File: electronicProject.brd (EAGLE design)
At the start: 100.3 x 79.7 mm, 15 parts

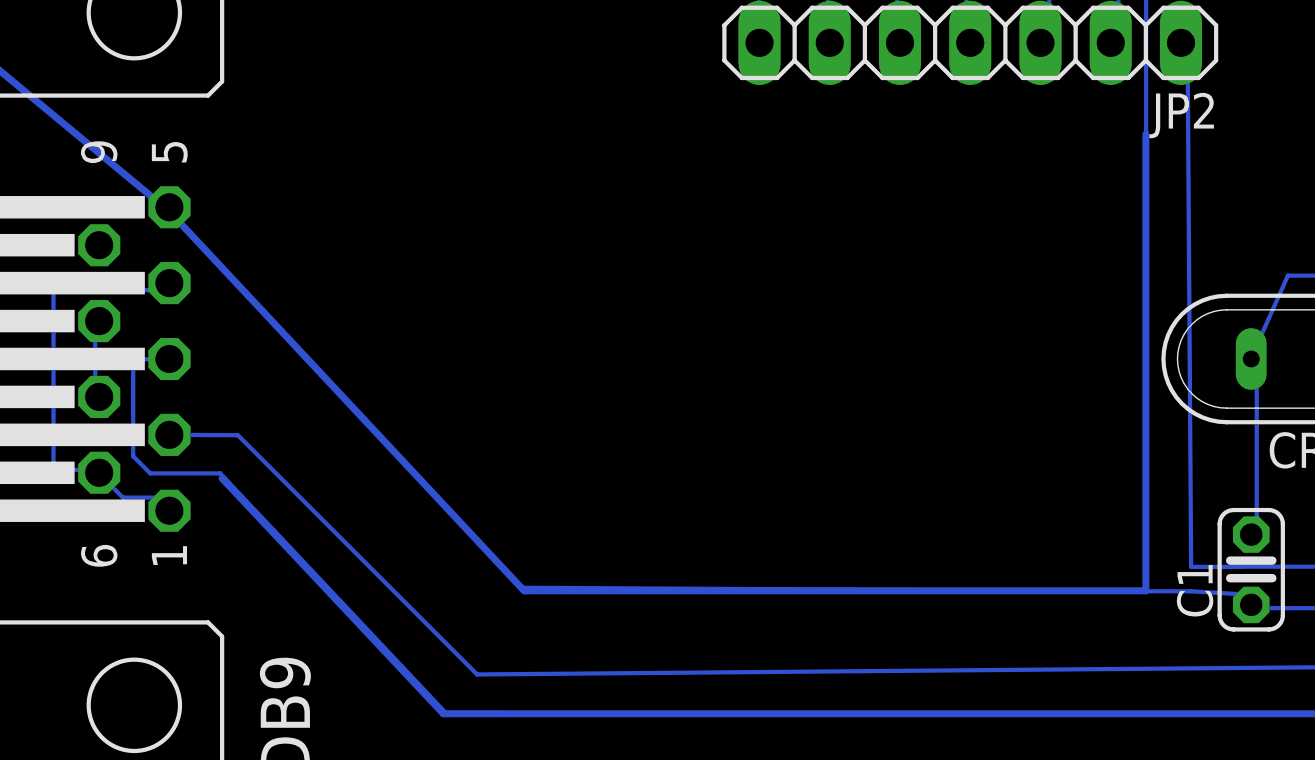
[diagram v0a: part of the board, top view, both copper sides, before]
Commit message: Update PCB design
Add Group and names on PCB
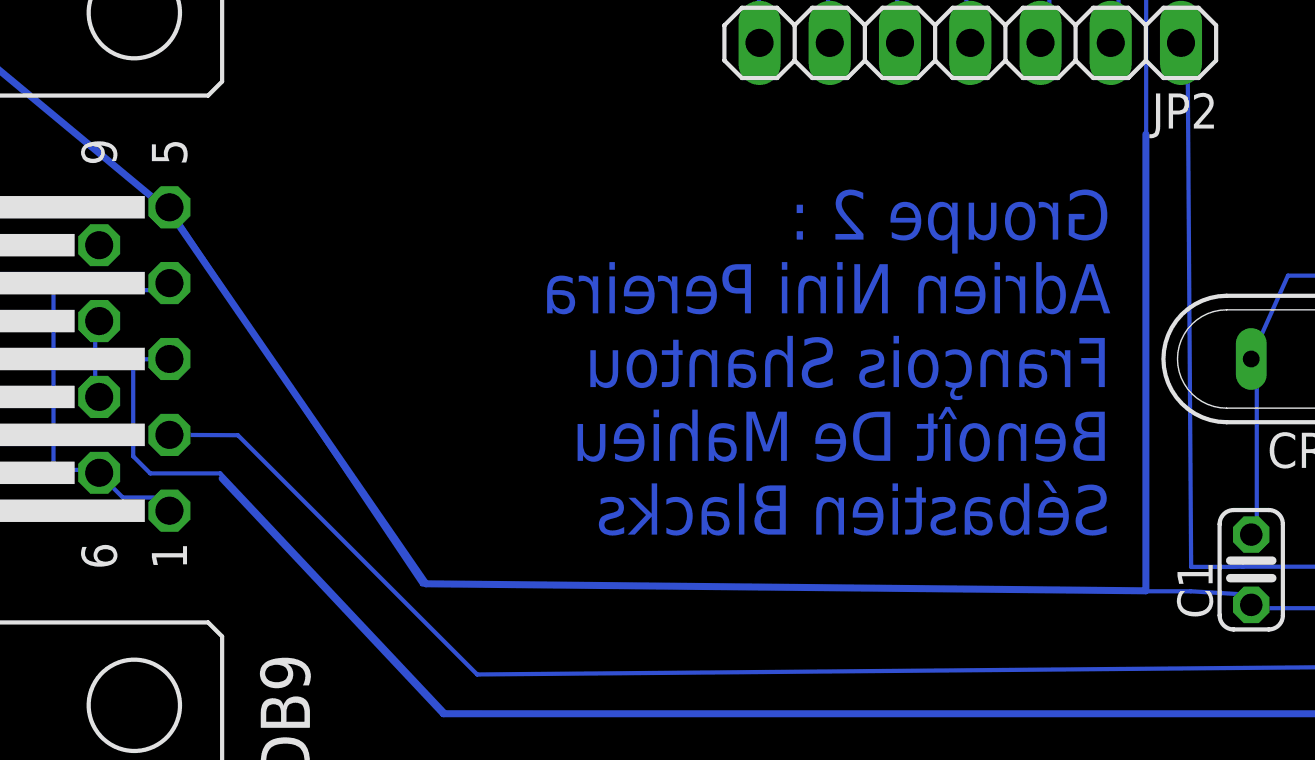
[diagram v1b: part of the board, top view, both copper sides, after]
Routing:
- net GND: track 630.3 -> 632.7 mm
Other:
- board text added: "Groupe 2 : Adrien Nini Pereira François Shantou Benoît De Mahieu Sébastien Blacks"
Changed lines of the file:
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@@
 </layers>
 <board>
+<fusionsync huburn="a.cGVyc29uYWw6dWUyYTAzMjA4" projecturn="a.cGVyc29uYWw6dWUyYTAzMjA4IzIwMTgwMjI2MTE5OTU2ODMx" f3durn="urn:adsk.wipprod:dm.lineage:Xcq5O81EQeOARa1FyexisA" pcbguid="bc2aa3ce-9b05-49e0-8871-5361d34968a8" lastpulledtime="" lastsyncedchangeguid="d90ede07-6539-4036-15fc-433ef894a95e"/>
 <plain>
 <wire x1="0" y1="0" x2="100.31" y2="0" width="0" layer="20"/>
@@
 <wire x1="100.31" y1="79.68" x2="0" y2="79.68" width="0" layer="20"/>
 <wire x1="0" y1="79.68" x2="0" y2="0" width="0" layer="20"/>
+<text x="45.72" y="10.16" size="1.778" layer="16" rot="MR0">Groupe 2 :
+Adrien Nini Pereira
+François Shantou
+Benoît De Mahieu
+Sébastien Blacks</text>
 </plain>
 <attributes>
@@
 <wire x1="14.5" y1="44" x2="14.6812" y2="44.1706" width="0.1524" layer="16"/>
 <wire x1="48.611" y1="8.111" x2="50.5" y2="8" width="0.1524" layer="16"/>
-<wire x1="24.373" y1="8.238" x2="47" y2="8.111" width="0.1524" layer="16"/>
+<wire x1="20.817" y1="8.365" x2="47" y2="8.111" width="0.1524" layer="16"/>
 <wire x1="47" y1="8.111" x2="48.611" y2="8.111" width="0.1524" layer="16"/>
-<wire x1="12" y1="21.5" x2="24.373" y2="8.238" width="0.1524" layer="16"/>
+<wire x1="12" y1="21.5" x2="20.817" y2="8.365" width="0.1524" layer="16"/>
 <wire x1="50.5" y1="8" x2="50.8" y2="7.62" width="0.1524" layer="16"/>
 <wire x1="12" y1="21.5" x2="11.684" y2="21.9964" width="0.1524" layer="16"/>
@@
 <wire x1="5.08" y1="41.656" x2="4.953" y2="27.432" width="0.254" layer="16"/>
 <wire x1="4.953" y1="27.432" x2="11.684" y2="21.844" width="0.254" layer="16"/>
-<wire x1="11.684" y1="21.844" x2="24.511" y2="8.128" width="0.254" layer="16"/>
-<wire x1="24.511" y1="8.128" x2="46.99" y2="8.128" width="0.254" layer="16"/>
+<wire x1="11.684" y1="21.844" x2="20.955" y2="8.382" width="0.254" layer="16"/>
+<wire x1="20.955" y1="8.382" x2="46.99" y2="8.128" width="0.254" layer="16"/>
 <wire x1="46.99" y1="8.128" x2="46.99" y2="24.638" width="0.254" layer="16"/>
 <wire x1="95.25" y1="36.83" x2="91.44" y2="36.83" width="0.254" layer="16"/>
@@
 </drawing>
 <compatibility>
+<note version="6.3" minversion="6.2.2" severity="warning">
+Since Version 6.2.2 text objects can contain more than one line,
+which will not be processed correctly with this version.
+</note>
 <note version="8.2" severity="warning">
 Since Version 8.2, EAGLE supports online libraries. The ids
@@
 </note>
 <note version="8.3" severity="warning">
+Since Version 8.3, EAGLE supports Fusion synchronisation.
+This feature will not be available in this version and saving
+the document will break the link to the Fusion PCB feature.
+</note>
+<note version="8.3" severity="warning">

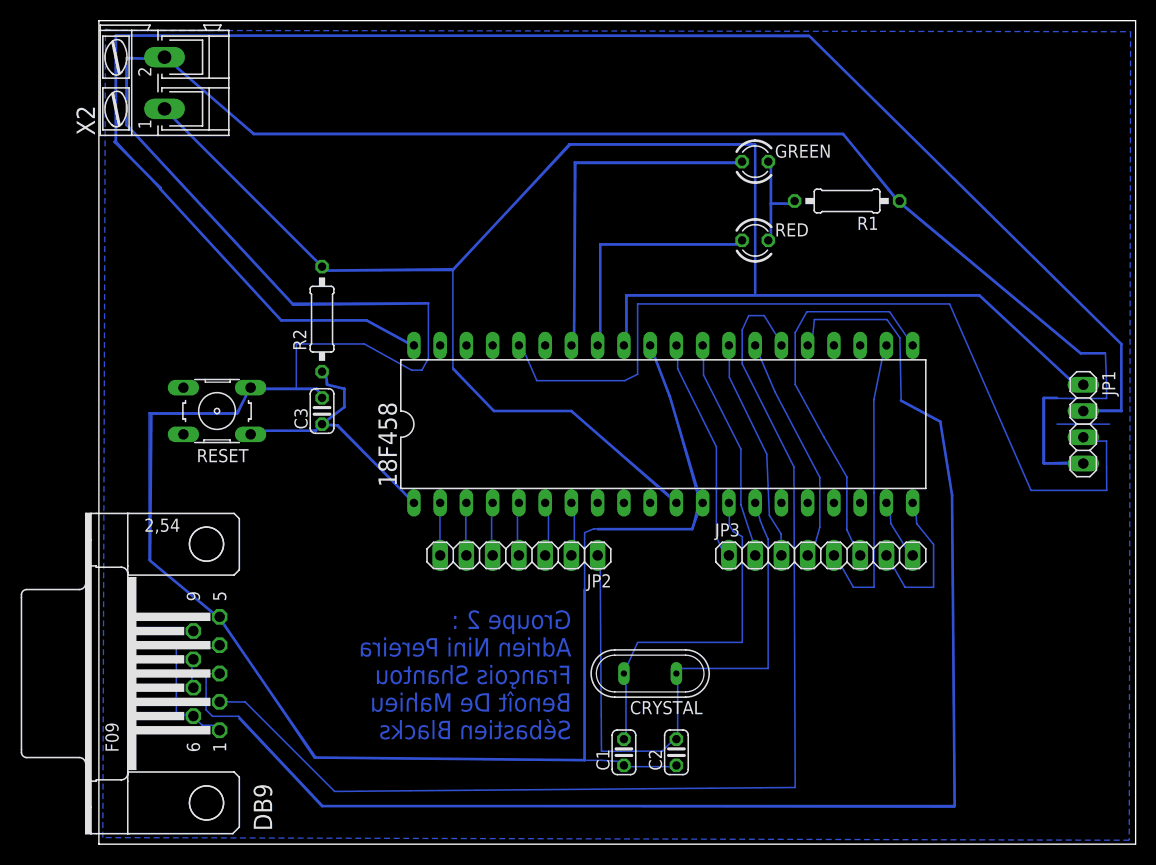
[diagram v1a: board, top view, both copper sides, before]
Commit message: Board UPDATE
Correction sonde à ultrasons (rotation 180°)
Reroutage des pattes de la sonde
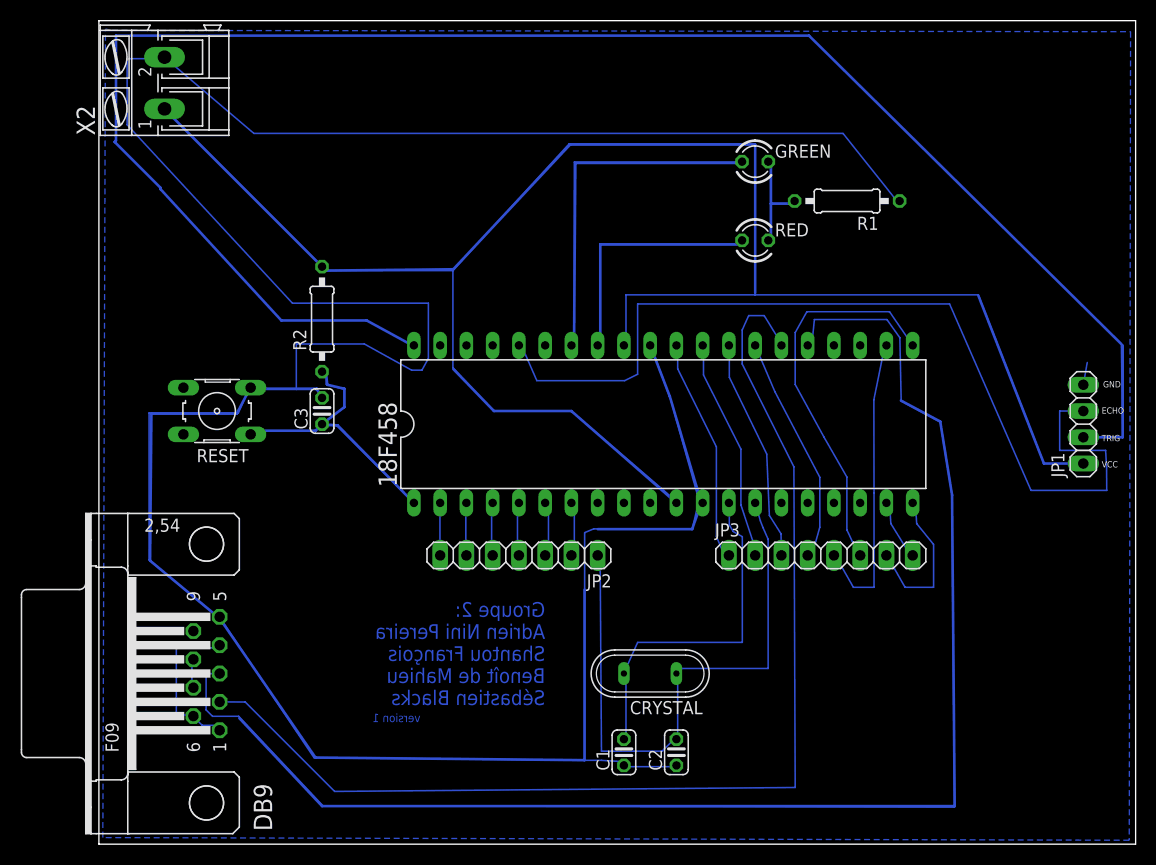
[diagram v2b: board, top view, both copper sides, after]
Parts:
- turned JP1 to 90 degrees
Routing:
- net GND: track 632.7 -> 423.1 mm
- net N$13: track 114.1 -> 0.00 mm
- net TRIG: track 219.3 -> 178.3 mm
- net VCC: track 320.4 -> 293.1 mm
- net ECHO: track 85.0 -> 92.2 mm
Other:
- board text added: "ECHO"
- board text added: "GND"
- board text added: "Groupe 2: Adrien Nini Pereira Shantou François Benoît de Mahieu Sébastien Blacks"
- board text added: "TRIG"
- board text added: "VCC"
- board text added: "version 1"
- board text removed: "Groupe 2 : Adrien Nini Pereira François Shantou Benoît De Mahieu Sébastien Blacks"

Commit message: final design
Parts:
- JP2: device pinhead:1X07 -> pinhead:1X06
- moved JP2 1.27 mm to (39.4, 27.9)
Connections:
- net N$10: now also JP2.3; no longer JP2.4
- net N$14: now also JP2.2; no longer JP2.3
- net N$15: now also JP2.1; no longer JP2.2
- net N$17: no longer JP2.1
- net N$4: now also JP2.6; no longer JP2.7
- net N$5: now also JP2.5; no longer JP2.6
- net N$6: now also JP2.4; no longer JP2.5
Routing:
- net N$17: track 58.7 -> 39.7 mm
- net N$10: track 5.29 -> 10.5 mm
- net N$6: track 5.22 -> 10.3 mm
- net N$5: track 5.15 -> 10.2 mm
- net N$4: track 5.09 -> 10.2 mm
- net N$14: track 5.65 -> 10.6 mm
- net N$15: track 5.57 -> 10.5 mm
- net TRIG: track 178.3 -> 178.9 mm
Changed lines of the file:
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@@
 </element>
 <element name="JP3" library="pinhead" library_urn="urn:adsk.eagle:library:325" package="1X08" package3d_urn="urn:adsk.eagle:package:22409/2" value="" x="69.85" y="27.94"/>
-<element name="JP2" library="pinhead" library_urn="urn:adsk.eagle:library:325" package="1X07" package3d_urn="urn:adsk.eagle:package:22477/2" value="" x="40.64" y="27.94" rot="R180"/>
+<element name="JP2" library="pinhead" library_urn="urn:adsk.eagle:library:325" package="1X06" package3d_urn="urn:adsk.eagle:package:22472/2" value="" x="39.37" y="27.94" rot="R180"/>
 </elements>
 <signals>
@@
 <wire x1="5.969" y1="63.373" x2="17.653" y2="50.673" width="0.254" layer="16"/>
 <wire x1="17.653" y1="50.673" x2="25.908" y2="50.673" width="0.254" layer="16"/>
-<wire x1="25.908" y1="50.673" x2="30.099" y2="48.387" width="0.254" layer="16"/>
-<wire x1="30.48" y1="48.26" x2="30.099" y2="48.387" width="0" layer="19" extent="16-16"/>
+<wire x1="25.908" y1="50.673" x2="29.975196875" y2="48.454528125" width="0.254" layer="16"/>
+<wire x1="29.975196875" y1="48.454528125" x2="30.099" y2="48.387" width="0.254" layer="16"/>
+<wire x1="30" y1="48.5" x2="30.25" y2="48.5" width="0.1524" layer="16"/>
+<wire x1="30.25" y1="48.5" x2="30.48" y2="48.26" width="0.1524" layer="16"/>
+<wire x1="30" y1="48.5" x2="29.975196875" y2="48.454528125" width="0.1524" layer="16"/>
 </signal>
 <signal name="ECHO">
@@
 <wire x1="82.532" y1="33.881" x2="81.413" y2="40.842" width="0.1524" layer="16"/>
 <wire x1="82.786" y1="3.587" x2="82.532" y2="33.881" width="0.1524" layer="16"/>
-<wire x1="21.675" y1="3.714" x2="82.786" y2="3.587" width="0.1524" layer="16"/>
+<wire x1="21.675" y1="3.714" x2="40.999840625" y2="3.673840625" width="0.1524" layer="16"/>
+<wire x1="40.999840625" y1="3.673840625" x2="82.786" y2="3.587" width="0.1524" layer="16"/>
 <wire x1="13.524" y1="12.373" x2="21.675" y2="3.714" width="0.1524" layer="16"/>
 <wire x1="10.992" y1="12.373" x2="13.524" y2="12.373" width="0.1524" layer="16"/>
@@
 <wire x1="11.5" y1="16.5" x2="11.684" y2="16.51" width="0.1524" layer="16"/>
 <wire x1="13.589" y1="12.192" x2="21.59" y2="3.683" width="0.254" layer="16"/>
-<wire x1="21.59" y1="3.683" x2="82.804" y2="3.683" width="0.254" layer="16"/>
+<wire x1="21.59" y1="3.683" x2="41" y2="3.683" width="0.254" layer="16"/>
+<wire x1="41" y1="3.683" x2="82.804" y2="3.683" width="0.254" layer="16"/>
 <wire x1="82.804" y1="3.683" x2="82.55" y2="33.782" width="0.254" layer="16"/>
 <wire x1="82.55" y1="33.782" x2="81.407" y2="40.894" width="0.254" layer="16"/>
 <wire x1="81.407" y1="40.894" x2="77.597" y2="42.926" width="0.254" layer="16"/>
-<wire x1="77.627" y1="42.874" x2="77.597" y2="42.926" width="0" layer="19" extent="16-16"/>
+<wire x1="41" y1="3.75" x2="41" y2="3.683" width="0.1524" layer="16"/>
+<wire x1="41" y1="3.75" x2="40.999840625" y2="3.673840625" width="0.1524" layer="16"/>
 </signal>
 <signal name="N$16">
@@
 <signal name="N$4">
 <contactref element="18F458" pad="2"/>
-<contactref element="JP2" pad="7"/>
+<contactref element="JP2" pad="6"/>
 <wire x1="33" y1="28" x2="33" y2="33" width="0.1524" layer="16"/>
 <wire x1="33" y1="33" x2="33.02" y2="33.02" width="0.1524" layer="16"/>
 <wire x1="33" y1="28" x2="33.02" y2="27.94" width="0.1524" layer="16"/>
+<wire x1="33.02" y1="27.94" x2="33.02" y2="33.02" width="0.254" layer="16"/>
 </signal>
 <signal name="N$5">
-<contactref element="JP2" pad="6"/>
 <contactref element="18F458" pad="3"/>
+<contactref element="JP2" pad="5"/>
 <wire x1="35.5" y1="28" x2="35.5" y2="33" width="0.1524" layer="16"/>
 <wire x1="35.5" y1="33" x2="35.56" y2="33.02" width="0.1524" layer="16"/>
 <wire x1="35.5" y1="28" x2="35.56" y2="27.94" width="0.1524" layer="16"/>
+<wire x1="35.56" y1="27.94" x2="35.56" y2="33.02" width="0.254" layer="16"/>
 </signal>
 <signal name="N$6">
 <contactref element="18F458" pad="4"/>
-<contactref element="JP2" pad="5"/>
+<contactref element="JP2" pad="4"/>
 <wire x1="38" y1="28" x2="38" y2="33" width="0.1524" layer="16"/>
 <wire x1="38" y1="33" x2="38.1" y2="33.02" width="0.1524" layer="16"/>
 <wire x1="38" y1="28" x2="38.1" y2="27.94" width="0.1524" layer="16"/>
+<wire x1="38.1" y1="27.94" x2="38.1" y2="33.02" width="0.254" layer="16"/>
 </signal>
 <signal name="N$10">
-<contactref element="JP2" pad="4"/>
 <contactref element="18F458" pad="5"/>
-<wire x1="40.5" y1="28" x2="40.5" y2="33" width="0.1524" layer="16"/>
 <wire x1="40.5" y1="33" x2="40.64" y2="33.02" width="0.1524" layer="16"/>
-<wire x1="40.5" y1="28" x2="40.64" y2="27.94" width="0.1524" layer="16"/>
+<contactref element="JP2" pad="3"/>
+<wire x1="40.75" y1="28" x2="40.75" y2="33" width="0.1524" layer="16"/>
+<wire x1="40.75" y1="33" x2="40.64" y2="33.02" width="0.1524" layer="16"/>
+<wire x1="40.75" y1="28" x2="40.64" y2="27.94" width="0.1524" layer="16"/>
+<wire x1="40.64" y1="27.94" x2="40.64" y2="33.02" width="0.254" layer="16"/>
 </signal>
 <signal name="N$14">
 <contactref element="18F458" pad="6"/>
-<contactref element="JP2" pad="3"/>
-<wire x1="43.5" y1="28" x2="43.5" y2="33" width="0.1524" layer="16"/>
 <wire x1="43.5" y1="33" x2="43.18" y2="33.02" width="0.1524" layer="16"/>
-<wire x1="43.5" y1="28" x2="43.18" y2="27.94" width="0.1524" layer="16"/>
+<contactref element="JP2" pad="2"/>
+<wire x1="43.25" y1="28" x2="43.25" y2="33" width="0.1524" layer="16"/>
+<wire x1="43.25" y1="33" x2="43.18" y2="33.02" width="0.1524" layer="16"/>
+<wire x1="43.25" y1="28" x2="43.18" y2="27.94" width="0.1524" layer="16"/>
+<wire x1="43.18" y1="27.94" x2="43.18" y2="33.02" width="0.254" layer="16"/>
 </signal>
 <signal name="N$15">
-<contactref element="JP2" pad="2"/>
 <contactref element="18F458" pad="7"/>
-<wire x1="46" y1="28" x2="46" y2="33" width="0.1524" layer="16"/>
 <wire x1="46" y1="33" x2="45.72" y2="33.02" width="0.1524" layer="16"/>
-<wire x1="46" y1="28" x2="45.72" y2="27.94" width="0.1524" layer="16"/>
+<contactref element="JP2" pad="1"/>
+<wire x1="45.75" y1="28" x2="45.75" y2="33" width="0.1524" layer="16"/>
+<wire x1="45.75" y1="33" x2="45.72" y2="33.02" width="0.1524" layer="16"/>
+<wire x1="45.75" y1="28" x2="45.72" y2="27.94" width="0.1524" layer="16"/>
+<wire x1="45.72" y1="27.94" x2="45.72" y2="33.02" width="0.254" layer="16"/>
 </signal>
 <signal name="N$17">
-<contactref element="JP2" pad="1"/>
 <contactref element="CRYSTAL" pad="1"/>
 <contactref element="18F458" pad="14"/>
@@
 <wire x1="56" y1="17" x2="64.754" y2="17" width="0.1524" layer="16"/>
 <wire x1="56" y1="17" x2="55.88" y2="16.51" width="0.1524" layer="16"/>
-<wire x1="48.627" y1="8.992" x2="48.5" y2="27.5" width="0.1524" layer="16"/>
 <wire x1="50.127" y1="8.992" x2="48.627" y2="8.992" width="0.1524" layer="16"/>
 <wire x1="50.5" y1="9" x2="50.127" y2="8.992" width="0.1524" layer="16"/>
 <wire x1="54.5" y1="9" x2="50.5" y2="9" width="0.1524" layer="16"/>
 <wire x1="55.5" y1="10" x2="54.5" y2="9" width="0.1524" layer="16"/>
-<wire x1="48.5" y1="27.5" x2="48.26" y2="27.94" width="0.1524" layer="16"/>
 <wire x1="55.5" y1="10" x2="55.88" y2="10.16" width="0.1524" layer="16"/>
 </signal>
